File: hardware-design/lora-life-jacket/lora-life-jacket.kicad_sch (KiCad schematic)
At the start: 18 parts, among them J1 7.4_BATT_IN, J2 RC522 CONNECTOR, J3 WATER LEVEL SENSOR, SW1 ON/OFF, SW2 PANIC_BTN, U1 NODEMCU-32S, U3 AMS1117-3.3, U4 RA-01H

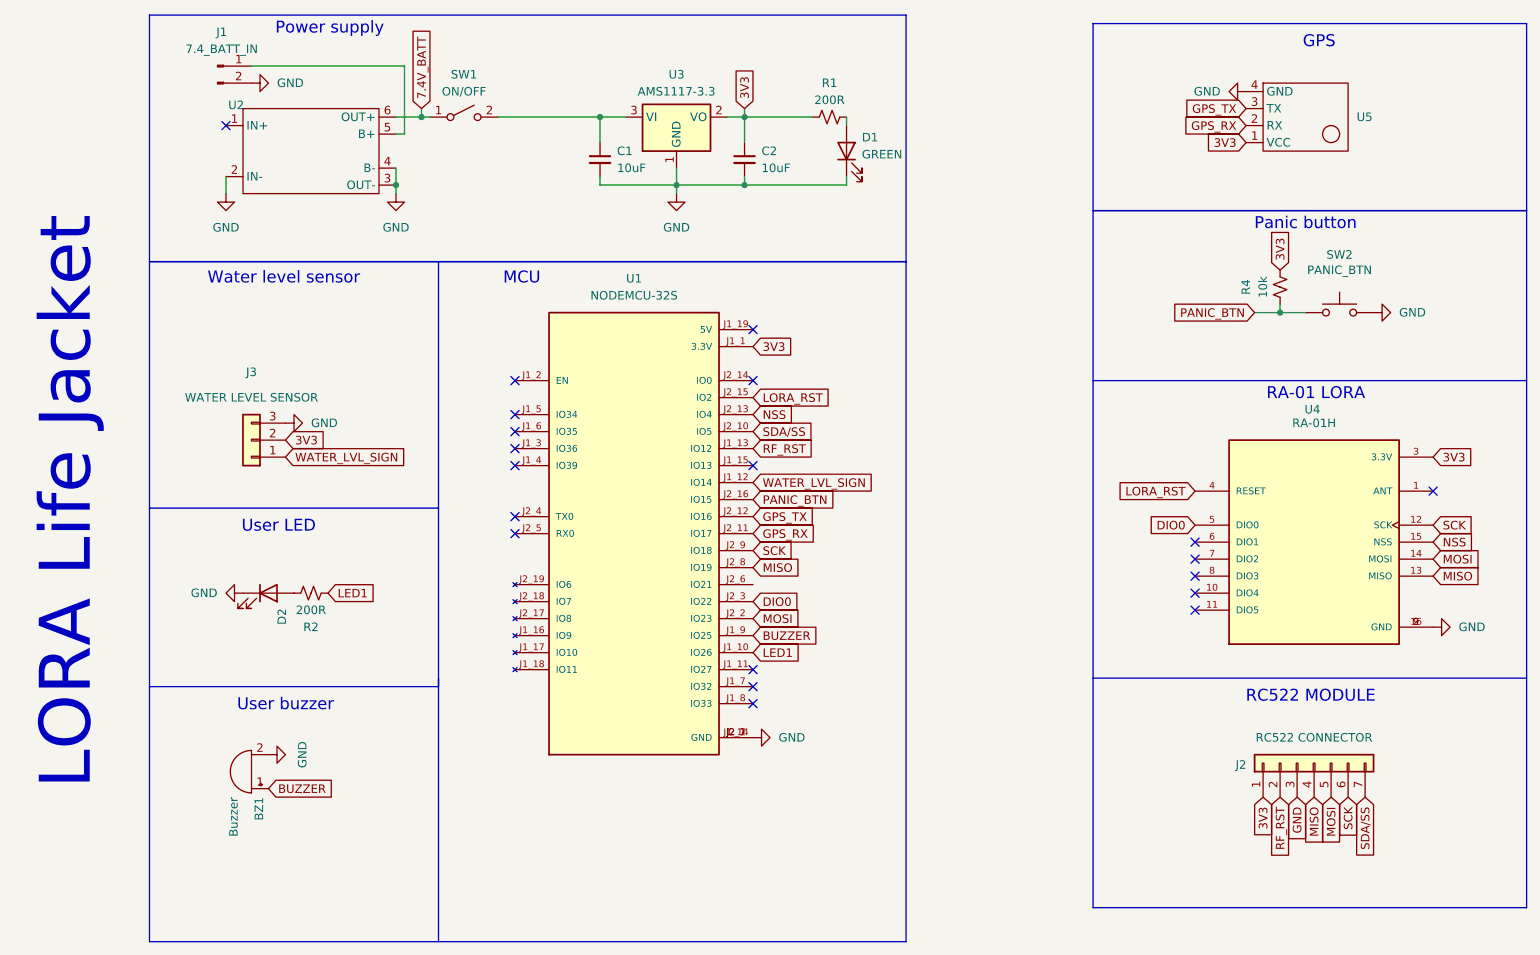
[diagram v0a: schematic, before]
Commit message: adds base station
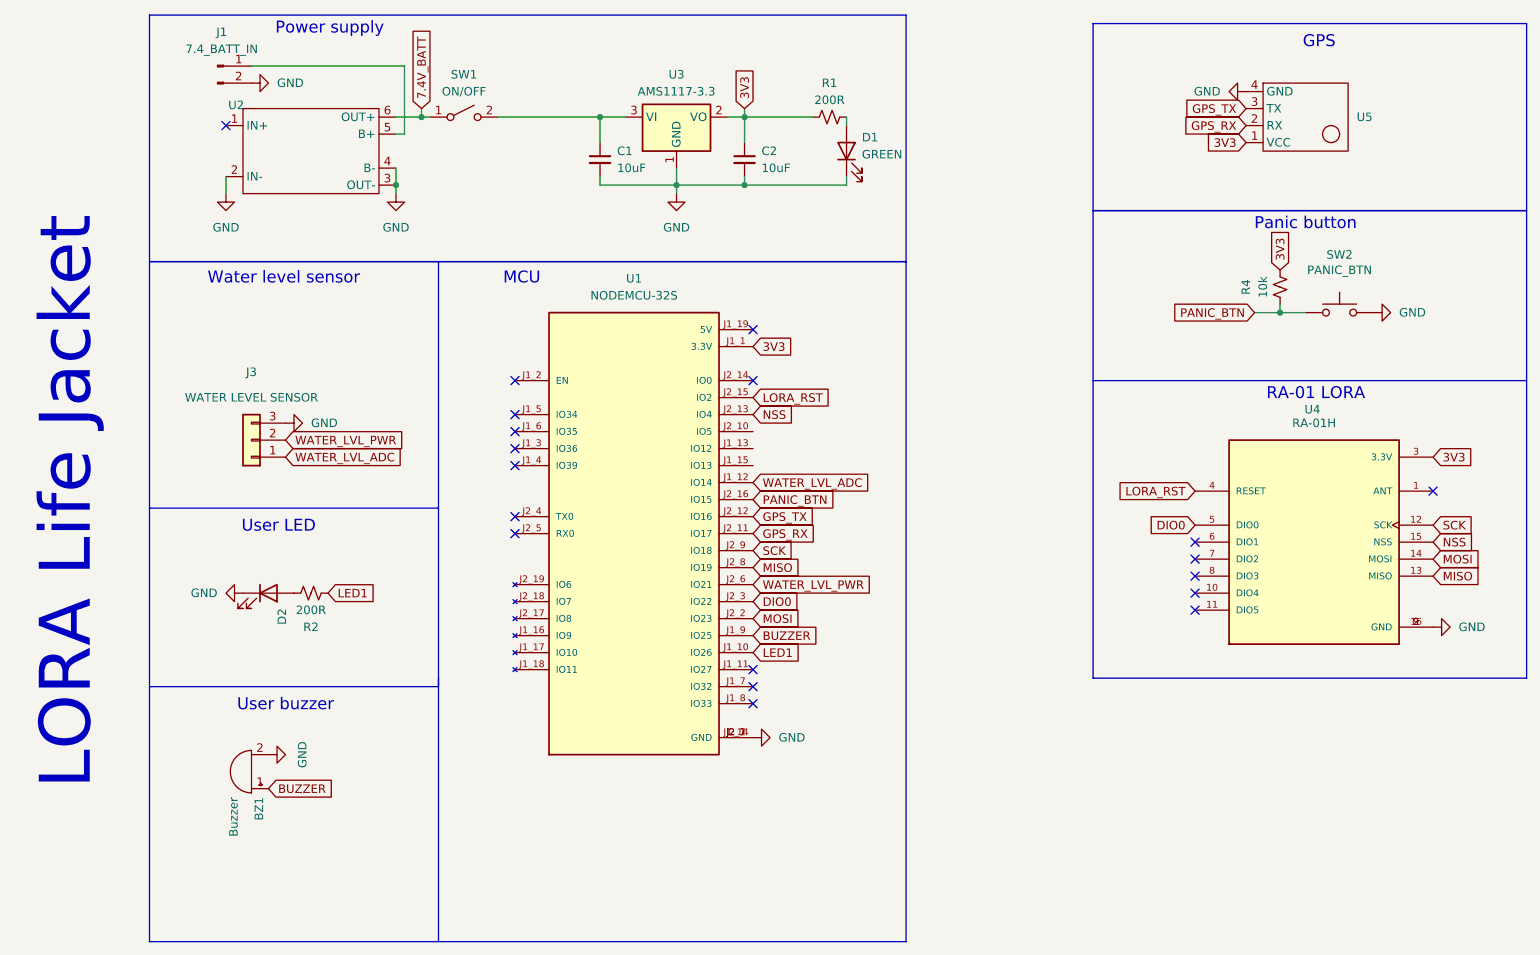
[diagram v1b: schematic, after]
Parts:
- removed J2: RC522 CONNECTOR, symbol Connector_Generic:Conn_01x07
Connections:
- net 3V3: no longer J3.2 (Pin_2)
- net WATER_LVL_PWR: now reaches U1.J2_6 (IO21)
- net WATER_LVL_PWR: now also J3.2 (Pin_2)
- net RF_RST: no longer names the net of U1.J1_13 (IO12)
- net SDA/SS: no longer names the net of U1.J2_10 (IO5)
- net WATER_LVL_SIGN renamed WATER_LVL_ADC
- no-connect marks 20 -> 19
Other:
- note removed: "RC522 MODULE"

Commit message: adds PCB tracks
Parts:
- BZ1: footprint (none) -> Buzzer_Beeper:MagneticBuzzer_ProSignal_ABI-010-RC
- C1, C2: footprint (none) -> Capacitor_THT:CP_Radial_D8.0mm_P3.80mm
- D1, D2: footprint (none) -> LED_THT:LED_D3.0mm
- J1: footprint (none) -> Connector_PinHeader_2.54mm:PinHeader_1x02_P2.54mm_Vertical
- J3: footprint (none) -> Connector_PinHeader_2.54mm:PinHeader_1x03_P2.54mm_Vertical
- R1, R2, R4: footprint (none) -> Resistor_THT:R_Axial_DIN0309_L9.0mm_D3.2mm_P15.24mm_Horizontal
- SW1: footprint (none) -> Button_Switch_THT:SW_Push_2P2T_Toggle_CK_PVA2OAH5xxxxxxV2
- SW2: footprint (none) -> Button_Switch_THT:SW_Tactile_Straight_KSL0Axx1LFTR
- U2: footprint (none) -> my-modules:TP4056-MODULE
- U5: footprint (none) -> my-modules:NEO-6M-GPS-MODULE
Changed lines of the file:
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@@
 			)
 		)
-		(property "Footprint" ""
+		(property "Footprint" "Button_Switch_THT:SW_Push_2P2T_Toggle_CK_PVA2OAH5xxxxxxV2"
 			(at 96.52 43.18 0)
 			(effects
@@
 			)
 		)
-		(property "Footprint" ""
+		(property "Footprint" "my-modules:TP4056-MODULE"
 			(at 64.77 40.386 0)
 			(effects
@@
 			)
 		)
-		(property "Footprint" ""
+		(property "Footprint" "Resistor_THT:R_Axial_DIN0309_L9.0mm_D3.2mm_P15.24mm_Horizontal"
 			(at 151.13 43.18 0)
 			(effects
@@
 			)
 		)
-		(property "Footprint" ""
+		(property "Footprint" "Resistor_THT:R_Axial_DIN0309_L9.0mm_D3.2mm_P15.24mm_Horizontal"
 			(at 218.44 68.58 0)
 			(effects
@@
 			)
 		)
-		(property "Footprint" ""
+		(property "Footprint" "LED_THT:LED_D3.0mm"
 			(at 67.31 114.3 0)
 			(effects
@@
 			)
 		)
-		(property "Footprint" ""
+		(property "Footprint" "Connector_PinHeader_2.54mm:PinHeader_1x02_P2.54mm_Vertical"
 			(at 59.69 35.56 0)
 			(effects
@@
 			)
 		)
-		(property "Footprint" ""
+		(property "Footprint" "LED_THT:LED_D3.0mm"
 			(at 153.67 48.26 0)
 			(effects
@@
 			)
 		)
-		(property "Footprint" ""
+		(property "Footprint" "Connector_PinHeader_2.54mm:PinHeader_1x03_P2.54mm_Vertical"
 			(at 64.77 91.44 0)
 			(effects
@@
 			)
 		)
-		(property "Footprint" ""
+		(property "Footprint" "my-modules:NEO-6M-GPS-MODULE"
 			(at 215.9 39.37 0)
 			(effects
@@
 			)
 		)
-		(property "Footprint" ""
+		(property "Footprint" "Buzzer_Beeper:MagneticBuzzer_ProSignal_ABI-010-RC"
 			(at 65.405 143.51 90)
 			(effects
@@
 			)
 		)
-		(property "Footprint" ""
+		(property "Footprint" "Capacitor_THT:CP_Radial_D8.0mm_P3.80mm"
 			(at 116.84 49.53 0)
 			(effects
@@
 			)
 		)
-		(property "Footprint" ""
+		(property "Footprint" "Resistor_THT:R_Axial_DIN0309_L9.0mm_D3.2mm_P15.24mm_Horizontal"
 			(at 73.66 114.3 0)
 			(effects
@@
 			)
 		)
-		(property "Footprint" ""
+		(property "Footprint" "Capacitor_THT:CP_Radial_D8.0mm_P3.80mm"
 			(at 138.43 49.53 0)
 			(effects
@@
 			)
 		)
-		(property "Footprint" ""
+		(property "Footprint" "Button_Switch_THT:SW_Tactile_Straight_KSL0Axx1LFTR"
 			(at 227.33 67.31 0)
 			(effects
